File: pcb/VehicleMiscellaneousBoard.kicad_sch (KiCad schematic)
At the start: 0 parts

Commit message: Made symbol for OpenMV H7+.
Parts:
- added U1: OpenMV H7+, pcb:OpenMV_H7_Plus, symbol OpenMV_H7_Plus:OpenMV_H7_Plus
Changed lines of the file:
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@@
 	(generator_version "9.0")
 	(paper "A4")
+	(symbol
+		(lib_id "OpenMV_H7_Plus:OpenMV_H7_Plus")
+		(at 109.22 76.2 0)
+		(unit 1)
+		(exclude_from_sim no)
+		(in_bom yes)
+		(on_board yes)
+		(dnp no)
+		(fields_autoplaced yes)
+		(property "Reference" "U1"
+			(at 109.22 45.72 0)
+			(effects
+				(font
+					(size 1.27 1.27)
+				)
+			)
+		)
+		(property "Value" "OpenMV H7+"
+			(at 109.22 48.26 0)
+			(effects
+				(font
+					(size 1.27 1.27)
+				)
+			)
+		)
+		(property "Footprint" "pcb:OpenMV_H7_Plus"
+			(at 109.22 69.85 0)
+			(effects
+				(font
+					(size 1.27 1.27)
+				)
+				(hide yes)
+			)
+		)
+		(property "Datasheet" "https://openmv.io/products/openmv-cam-h7-plus"
+			(at 109.22 69.85 0)
+			(effects
+				(font
+					(size 1.27 1.27)
+				)
+				(hide yes)
+			)
+		)
+		(property "Description" ""
+			(at 109.22 69.85 0)
+			(effects
+				(font
+					(size 1.27 1.27)
+				)
+				(hide yes)
+			)
+		)
+		(pin "VIN"
+		)
+		(pin "+3.3V"
+		)
+		(pin "PB12"
+		)
+		(pin "PB11"
+		)
+		(pin "PA5"
+		)
+		(pin "GND"
+		)
+		(pin "SWO"
+		)
+		(pin "PB10"
+		)
+		(pin "FSYNC"
+		)
+		(pin "PG3"
+		)
+		(pin "PB14"
+		)
+		(pin "PB15"
+		)
+		(pin "BOOT"
+		)
+		(pin "PD13"
+		)
+		(pin "NRST"
+		)
+		(pin "SWC"
+		)
+		(pin "PD12"
+		)
+		(pin "PB13"
+		)
+		(pin "SWD"
+		)
+		(instances
+			(project ""
+				(path "/091a7226-d417-4b79-83fb-bb50ff9fd5b7"
+					(reference "U1")
+					(unit 1)
+				)
+			)
+		)
+	)
 	(sheet_instances
 		(path "/"

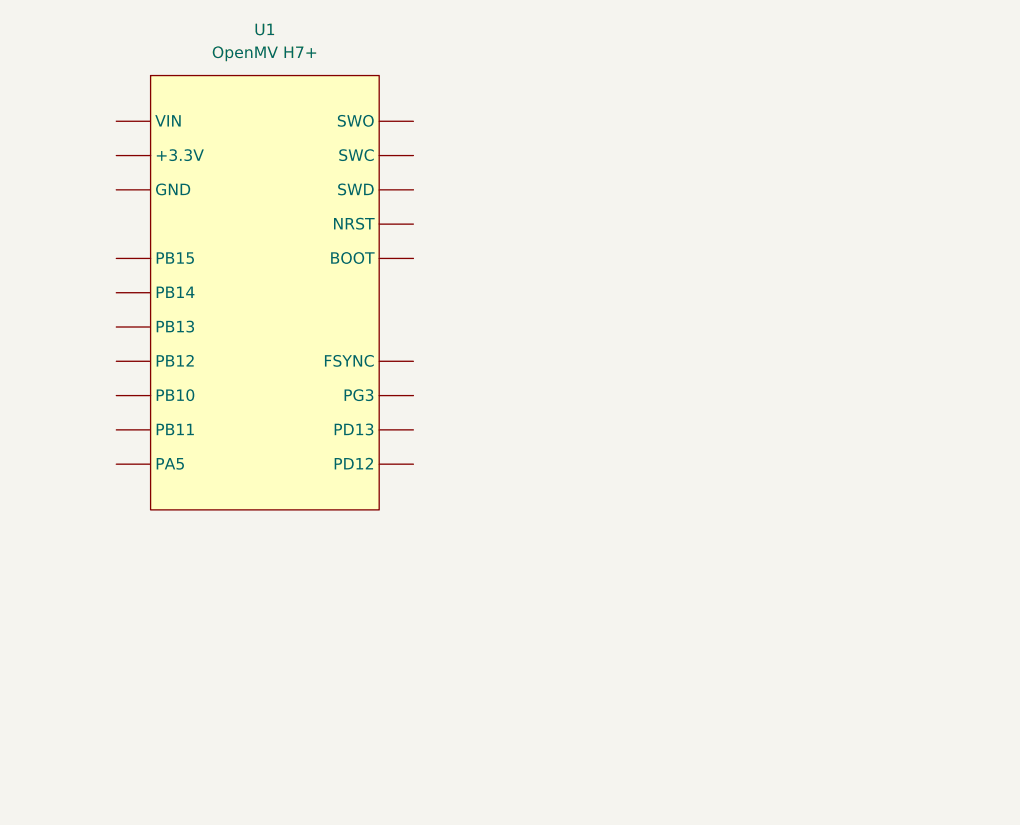
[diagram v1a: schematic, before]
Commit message: Added stack connector and XIAO ESP32 to `VehicleMiscellaneousBoard`.
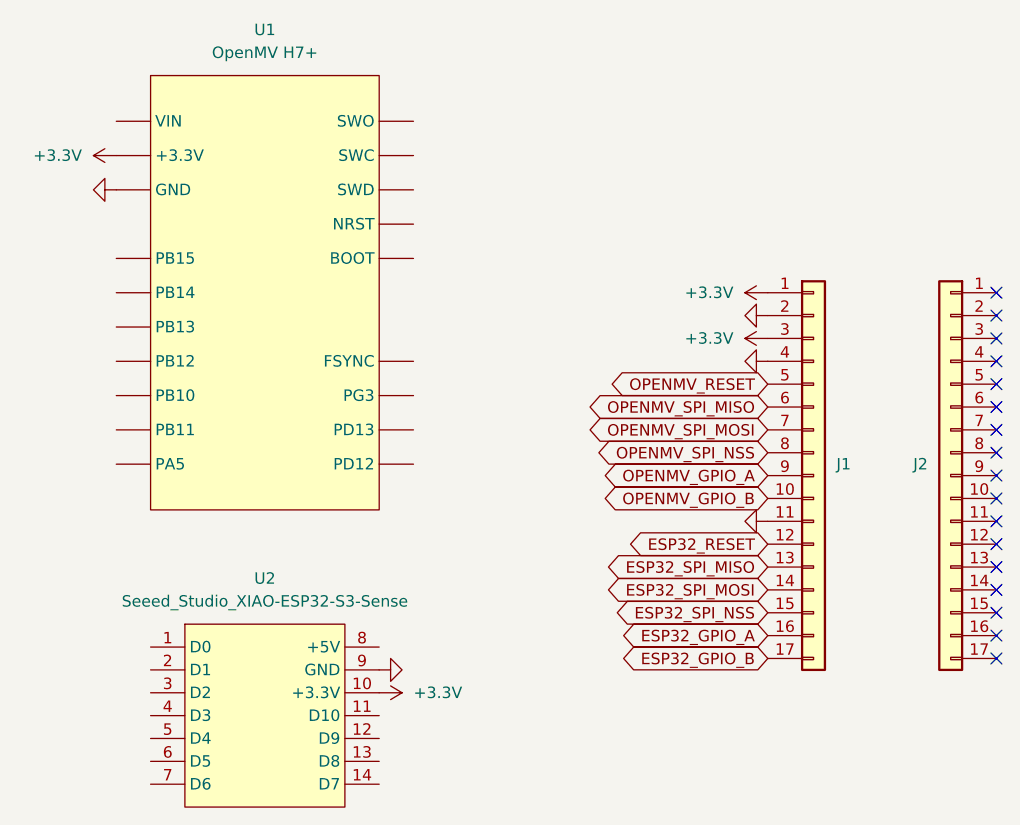
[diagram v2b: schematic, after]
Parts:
- added J1, J2: Conn_01x17, Connector_PinSocket_2.54mm:PinSocket_1x17_P2.54mm_Vertical, symbol Connector_Generic:Conn_01x17
- added U2: Seeed_Studio_XIAO-ESP32-S3-Sense, pcb:Seeed_Studio_XIAO_ESP32_S3, symbol Seeed_Studio_XIAO-ESP32-S3-Sense:Seeed_Studio_XIAO-ESP32-S3-Sense
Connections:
- net +3.3V: now reaches U1.+3.3V
- net +3.3V: now also J1.1 (Pin_1), J1.3 (Pin_3), U2.10 (+3.3V)
- net GND: now reaches U1.GND
- net GND: now also J1.11 (Pin_11), J1.2 (Pin_2), J1.4 (Pin_4), U2.9 (GND)
- new net ESP32_GPIO_A: J1.16 (Pin_16)
- new net ESP32_GPIO_B: J1.17 (Pin_17)
- new net ESP32_RESET: J1.12 (Pin_12)
- new net ESP32_SPI_MISO: J1.13 (Pin_13)
- new net ESP32_SPI_MOSI: J1.14 (Pin_14)
- new net ESP32_SPI_NSS: J1.15 (Pin_15)
- new net OPENMV_GPIO_A: J1.9 (Pin_9)
- new net OPENMV_GPIO_B: J1.10 (Pin_10)
- new net OPENMV_RESET: J1.5 (Pin_5)
- new net OPENMV_SPI_MISO: J1.6 (Pin_6)
- new net OPENMV_SPI_MOSI: J1.7 (Pin_7)
- new net OPENMV_SPI_NSS: J1.8 (Pin_8)
- no-connect marks 0 -> 17

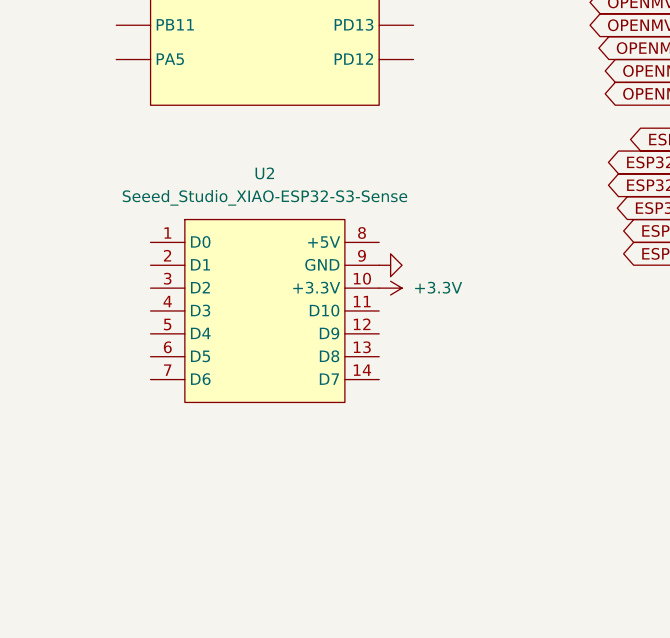
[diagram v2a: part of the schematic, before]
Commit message: Updated symbol and footprint of the XIAO ESP32 to account for the under pads.
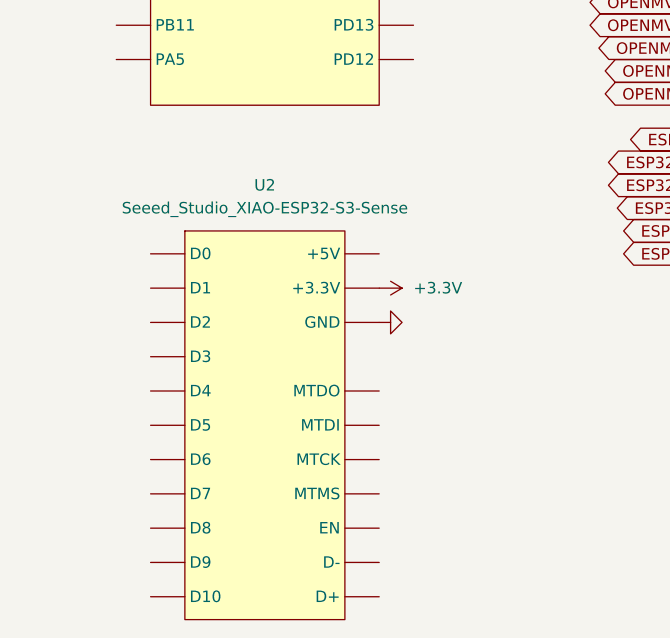
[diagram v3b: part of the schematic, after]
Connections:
- net +3.3V: now also U2.+3.3V; no longer U2.10 (+3.3V)
- net GND: now also U2.GND; no longer U2.9 (GND)

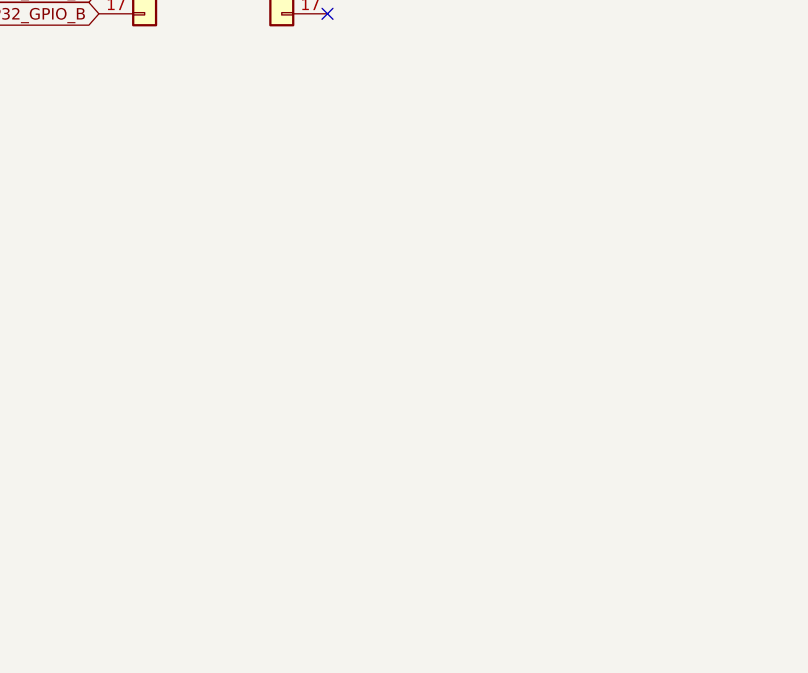
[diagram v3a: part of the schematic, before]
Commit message: Made `VehicleMiscellaneousBoard` switch to using the vehicle stack connector.
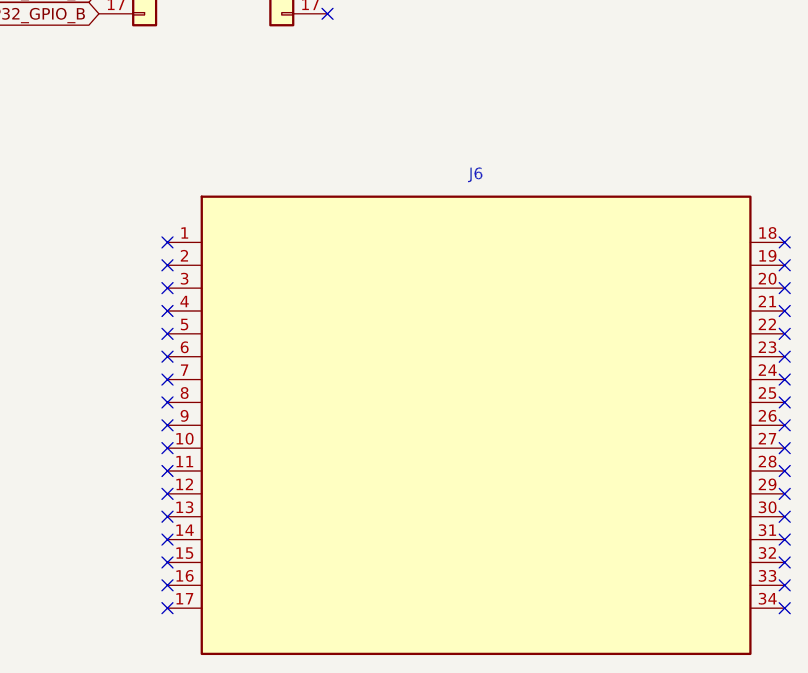
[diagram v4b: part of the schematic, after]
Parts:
- added J6: ~, pcb:VehicleStackConnector, symbol VehicleStackConnector:VehicleStackConnector
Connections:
- no-connect marks 17 -> 51
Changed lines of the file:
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@@
 	(paper "A4")
 	(no_connect
+		(at 172.72 140.97)
+	)
+	(no_connect
+		(at 172.72 161.29)
+	)
+	(no_connect
+		(at 172.72 148.59)
+	)
+	(no_connect
+		(at 241.3 166.37)
+	)
+	(no_connect
+		(at 241.3 140.97)
+	)
+	(no_connect
 		(at 190.5 74.93)
 	)
 	(no_connect
+		(at 241.3 163.83)
+	)
+	(no_connect
 		(at 190.5 77.47)
 	)
 	(no_connect
+		(at 241.3 153.67)
+	)
+	(no_connect
+		(at 172.72 143.51)
+	)
+	(no_connect
+		(at 172.72 181.61)
+	)
+	(no_connect
 		(at 190.5 105.41)
 	)
@@
 	)
 	(no_connect
+		(at 241.3 161.29)
+	)
+	(no_connect
+		(at 241.3 173.99)
+	)
+	(no_connect
+		(at 241.3 143.51)
+	)
+	(no_connect
 		(at 190.5 85.09)
 	)
 	(no_connect
+		(at 172.72 153.67)
+	)
+	(no_connect
 		(at 190.5 110.49)
 	)
@@
 	)
 	(no_connect
+		(at 172.72 146.05)
+	)
+	(no_connect
 		(at 190.5 102.87)
 	)
 	(no_connect
+		(at 172.72 171.45)
+	)
+	(no_connect
+		(at 172.72 151.13)
+	)
+	(no_connect
+		(at 241.3 181.61)
+	)
+	(no_connect
+		(at 241.3 179.07)
+	)
+	(no_connect
 		(at 190.5 107.95)
 	)
@@
 	)
 	(no_connect
+		(at 241.3 171.45)
+	)
+	(no_connect
+		(at 172.72 168.91)
+	)
+	(no_connect
 		(at 190.5 80.01)
 	)
 	(no_connect
+		(at 241.3 168.91)
+	)
+	(no_connect
+		(at 172.72 179.07)
+	)
+	(no_connect
+		(at 172.72 163.83)
+	)
+	(no_connect
 		(at 190.5 82.55)
 	)
 	(no_connect
+		(at 172.72 173.99)
+	)
+	(no_connect
 		(at 190.5 92.71)
 	)
 	(no_connect
+		(at 241.3 176.53)
+	)
+	(no_connect
+		(at 172.72 156.21)
+	)
+	(no_connect
 		(at 190.5 97.79)
 	)
@@
 	)
 	(no_connect
+		(at 241.3 151.13)
+	)
+	(no_connect
+		(at 241.3 156.21)
+	)
+	(no_connect
+		(at 241.3 146.05)
+	)
+	(no_connect
+		(at 172.72 166.37)
+	)
+	(no_connect
+		(at 172.72 158.75)
+	)
+	(no_connect
 		(at 190.5 95.25)
 	)
+	(no_connect
+		(at 241.3 148.59)
+	)
+	(no_connect
+		(at 172.72 176.53)
+	)
+	(no_connect
+		(at 241.3 158.75)
+	)
 	(global_label "ESP32_GPIO_B"
 		(shape bidirectional)
@@
 			)
 		)
+	)
+	(symbol
+		(lib_id "VehicleStackConnector:VehicleStackConnector")
+		(at 176.53 135.89 0)
+		(unit 1)
+		(exclude_from_sim no)
+		(in_bom yes)
+		(on_board yes)
+		(dnp no)
+		(fields_autoplaced yes)
+		(property "Reference" "J6"
+			(at 207.01 133.35 0)
+			(effects
+				(font
+					(size 1.27 1.27)
+				)
+			)
+		)
+		(property "Value" "~"
+			(at 175.26 135.89 0)
+			(effects
+				(font
+					(size 1.27 1.27)
+				)
+				(hide yes)
+			)
+		)
+		(property "Footprint" "pcb:VehicleStackConnector"
+			(at 175.26 135.89 0)
+			(effects
+				(font
+					(size 1.27 1.27)
+				)
+				(hide yes)
+			)
+		)
+		(property "Datasheet" ""
+			(at 175.26 135.89 0)
+			(effects
+				(font
+					(size 1.27 1.27)
+				)
+				(hide yes)
+			)
+		)
+		(property "Description" ""
+			(at 175.26 135.89 0)
+			(effects
+				(font
+					(size 1.27 1.27)
+				)
+				(hide yes)
+			)
+		)
+		(pin "12"
+		)
+		(pin "30"
+		)
+		(pin "8"
+		)
+		(pin "23"
+		)
+		(pin "22"
+		)
+		(pin "19"
+		)
+		(pin "17"
+		)
+		(pin "29"
+		)
+		(pin "14"
+		)
+		(pin "15"
+		)
+		(pin "26"
+		)
+		(pin "18"
+		)
+		(pin "32"
+		)
+		(pin "34"
+		)
+		(pin "1"
+		)
+		(pin "5"
+		)
+		(pin "25"
+		)
+		(pin "24"
+		)
+		(pin "31"
+		)
+		(pin "10"
+		)
+		(pin "21"
+		)
+		(pin "9"
+		)
+		(pin "27"
+		)
+		(pin "28"
+		)
+		(pin "20"
+		)
+		(pin "13"
+		)
+		(pin "16"
+		)
+		(pin "4"
+		)
+		(pin "2"
+		)
+		(pin "6"
+		)
+		(pin "3"
+		)
+		(pin "11"
+		)
+		(pin "7"
+		)
+		(pin "33"
+		)
+		(instances
+			(project "VehicleMiscellaneousBoard"
+				(path "/091a7226-d417-4b79-83fb-bb50ff9fd5b7"
+					(reference "J6")
+					(unit 1)
+				)
+			)
+		)
